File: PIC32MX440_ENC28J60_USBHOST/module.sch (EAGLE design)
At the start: 79 parts, among them IC1 IC_USBLC6-2, IC2 LM1117IMPX-3.3, IC4 ENC28J60, IC5 PIC32MX440FH, T1 BC847, U1 USD-SOCKETUSD, X1 22-23-2021, X2 CRYSTALS-NOGND-CFPX-217, X3 KUSBVX, X5 22-23-2021, Y1 CRYSTAL-GROUNDEDSMD-5X3.2, Y2 CRYSTAL-GROUNDEDSMD-5X3.2

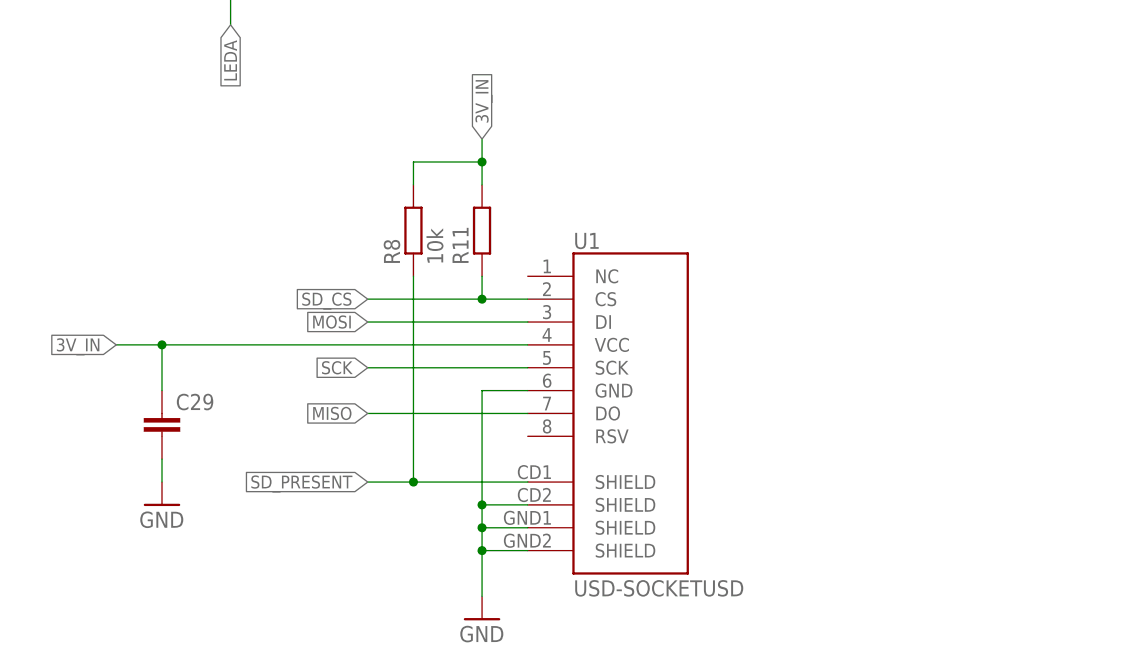
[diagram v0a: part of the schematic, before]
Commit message: MISO pull-ups added
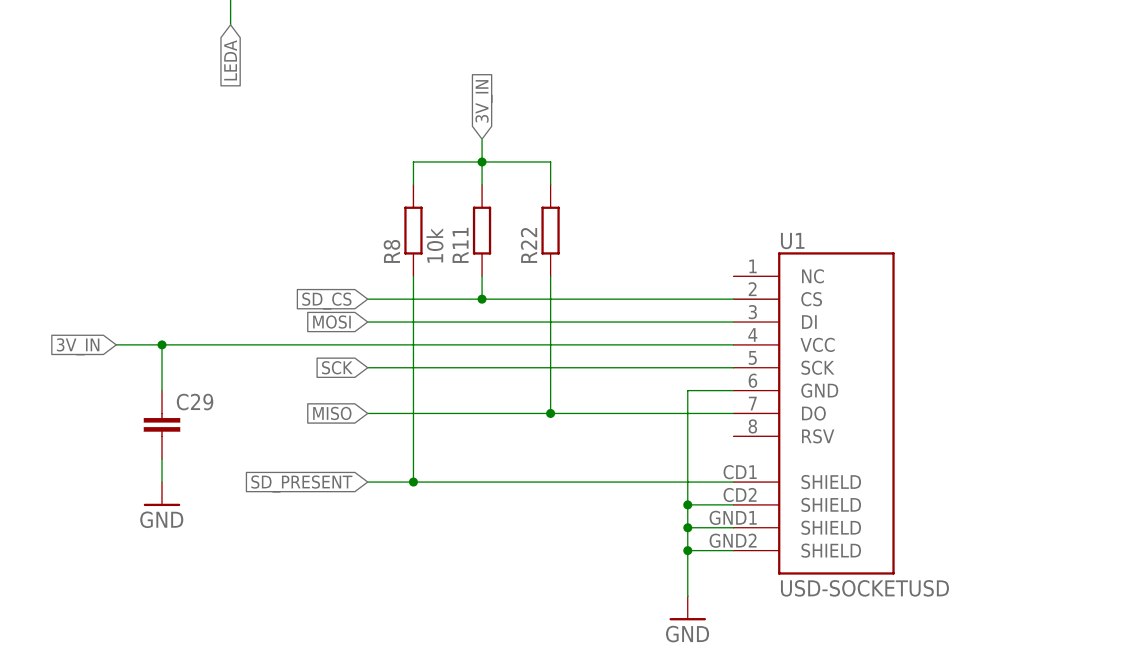
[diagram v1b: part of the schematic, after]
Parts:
- added R22: (no value), rcl:R-EU_R0603
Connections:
- net 3V_IN: now also R22.2
- net MISO: now also R22.1
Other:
- moved on the sheet: U1
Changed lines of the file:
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@@
 <part name="JP4" library="mw" deviceset="PINHD-2X5" device=""/>
 <part name="R15" library="rcl" deviceset="R-EU_" device="R0805"/>
+<part name="R22" library="rcl" deviceset="R-EU_" device="R0603"/>
 </parts>
 <sheets>
@@
 <instance part="R12" gate="G$1" x="73.66" y="83.82"/>
 <instance part="Y2" gate="G$1" x="73.66" y="157.48" rot="R90"/>
-<instance part="U1" gate="G$1" x="254" y="81.28"/>
-<instance part="GND47" gate="1" x="241.3" y="55.88"/>
+<instance part="U1" gate="G$1" x="276.86" y="81.28"/>
+<instance part="GND47" gate="1" x="264.16" y="55.88"/>
 <instance part="R11" gate="G$1" x="241.3" y="99.06" rot="R90"/>
 <instance part="C29" gate="G$1" x="205.74" y="78.74"/>
@@
 <instance part="JP4" gate="G$1" x="322.58" y="561.34"/>
 <instance part="R15" gate="G$1" x="96.52" y="513.08"/>
+<instance part="R22" gate="G$1" x="248.92" y="99.06" rot="R90"/>
 </instances>
 <busses>
@@
 <pinref part="GND47" gate="1" pin="GND"/>
 <pinref part="U1" gate="G$1" pin="SHIELD@4"/>
-<wire x1="241.3" y1="66.04" x2="241.3" y2="63.5" width="0.1524" layer="91"/>
-<wire x1="241.3" y1="63.5" x2="241.3" y2="58.42" width="0.1524" layer="91"/>
-<wire x1="246.38" y1="63.5" x2="241.3" y2="63.5" width="0.1524" layer="91"/>
-<junction x="241.3" y="63.5"/>
+<wire x1="264.16" y1="66.04" x2="264.16" y2="63.5" width="0.1524" layer="91"/>
+<wire x1="264.16" y1="63.5" x2="264.16" y2="58.42" width="0.1524" layer="91"/>
+<wire x1="269.24" y1="63.5" x2="264.16" y2="63.5" width="0.1524" layer="91"/>
+<junction x="264.16" y="63.5"/>
 <pinref part="U1" gate="G$1" pin="SHIELD@3"/>
-<wire x1="246.38" y1="66.04" x2="241.3" y2="66.04" width="0.1524" layer="91"/>
-<junction x="241.3" y="66.04"/>
+<wire x1="269.24" y1="66.04" x2="264.16" y2="66.04" width="0.1524" layer="91"/>
+<junction x="264.16" y="66.04"/>
 <pinref part="U1" gate="G$1" pin="GND"/>
-<wire x1="246.38" y1="81.28" x2="241.3" y2="81.28" width="0.1524" layer="91"/>
-<wire x1="241.3" y1="81.28" x2="241.3" y2="68.58" width="0.1524" layer="91"/>
+<wire x1="269.24" y1="81.28" x2="264.16" y2="81.28" width="0.1524" layer="91"/>
+<wire x1="264.16" y1="81.28" x2="264.16" y2="68.58" width="0.1524" layer="91"/>
 <pinref part="U1" gate="G$1" pin="SHIELD@2"/>
-<wire x1="241.3" y1="68.58" x2="241.3" y2="66.04" width="0.1524" layer="91"/>
-<wire x1="246.38" y1="68.58" x2="241.3" y2="68.58" width="0.1524" layer="91"/>
-<junction x="241.3" y="68.58"/>
+<wire x1="264.16" y1="68.58" x2="264.16" y2="66.04" width="0.1524" layer="91"/>
+<wire x1="269.24" y1="68.58" x2="264.16" y2="68.58" width="0.1524" layer="91"/>
+<junction x="264.16" y="68.58"/>
 </segment>
 <segment>
@@
 <segment>
 <pinref part="U1" gate="G$1" pin="SCK"/>
-<wire x1="246.38" y1="83.82" x2="228.6" y2="83.82" width="0.1524" layer="91"/>
+<wire x1="269.24" y1="83.82" x2="228.6" y2="83.82" width="0.1524" layer="91"/>
 <label x="228.6" y="83.82" size="1.4224" layer="95" rot="R180" xref="yes"/>
 </segment>
@@
 <segment>
 <pinref part="U1" gate="G$1" pin="DO"/>
-<wire x1="246.38" y1="78.74" x2="228.6" y2="78.74" width="0.1524" layer="91"/>
+<wire x1="269.24" y1="78.74" x2="248.92" y2="78.74" width="0.1524" layer="91"/>
 <label x="228.6" y="78.74" size="1.4224" layer="95" rot="R180" xref="yes"/>
+<pinref part="R22" gate="G$1" pin="1"/>
+<wire x1="248.92" y1="78.74" x2="228.6" y2="78.74" width="0.1524" layer="91"/>
+<wire x1="248.92" y1="93.98" x2="248.92" y2="78.74" width="0.1524" layer="91"/>
+<junction x="248.92" y="78.74"/>
 </segment>
 <segment>
@@
 <segment>
 <pinref part="U1" gate="G$1" pin="DI"/>
-<wire x1="246.38" y1="88.9" x2="228.6" y2="88.9" width="0.1524" layer="91"/>
+<wire x1="269.24" y1="88.9" x2="228.6" y2="88.9" width="0.1524" layer="91"/>
 <label x="228.6" y="88.9" size="1.4224" layer="95" rot="R180" xref="yes"/>
 </segment>
@@
 <segment>
 <pinref part="U1" gate="G$1" pin="CS"/>
-<wire x1="246.38" y1="91.44" x2="241.3" y2="91.44" width="0.1524" layer="91"/>
+<wire x1="269.24" y1="91.44" x2="241.3" y2="91.44" width="0.1524" layer="91"/>
 <pinref part="R11" gate="G$1" pin="1"/>
 <wire x1="241.3" y1="91.44" x2="228.6" y2="91.44" width="0.1524" layer="91"/>
@@
 <segment>
 <pinref part="U1" gate="G$1" pin="SHIELD@1"/>
-<wire x1="246.38" y1="71.12" x2="233.68" y2="71.12" width="0.1524" layer="91"/>
+<wire x1="269.24" y1="71.12" x2="233.68" y2="71.12" width="0.1524" layer="91"/>
 <label x="228.6" y="71.12" size="1.4224" layer="95" rot="R180" xref="yes"/>
 <pinref part="R8" gate="G$1" pin="1"/>
@@
 <segment>
 <pinref part="U1" gate="G$1" pin="VCC"/>
-<wire x1="246.38" y1="86.36" x2="205.74" y2="86.36" width="0.1524" layer="91"/>
+<wire x1="269.24" y1="86.36" x2="205.74" y2="86.36" width="0.1524" layer="91"/>
 <pinref part="C29" gate="G$1" pin="1"/>
 <wire x1="205.74" y1="86.36" x2="200.66" y2="86.36" width="0.1524" layer="91"/>
@@
 <pinref part="R8" gate="G$1" pin="2"/>
 <wire x1="233.68" y1="106.68" x2="233.68" y2="104.14" width="0.1524" layer="91"/>
-</segment>
-<segment>
+<pinref part="R22" gate="G$1" pin="2"/>
+<wire x1="241.3" y1="106.68" x2="248.92" y2="106.68" width="0.1524" layer="91"/>
+<wire x1="248.92" y1="106.68" x2="248.92" y2="104.14" width="0.1524" layer="91"/>
+</segment>
+<segment>
